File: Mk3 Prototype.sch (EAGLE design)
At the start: 170 parts, among them IC2 CC3100, IC3 S25FL216K0PMFI011, IC4 STM32F401V, IC6 AP3419, J1 ZX62-AB-5PA(11), J2 SWD_SHROUD, J7 SFV30R-2STE1HLF, Q1 BSS84W, Q11 BSS84W, Q12 2N7002KW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

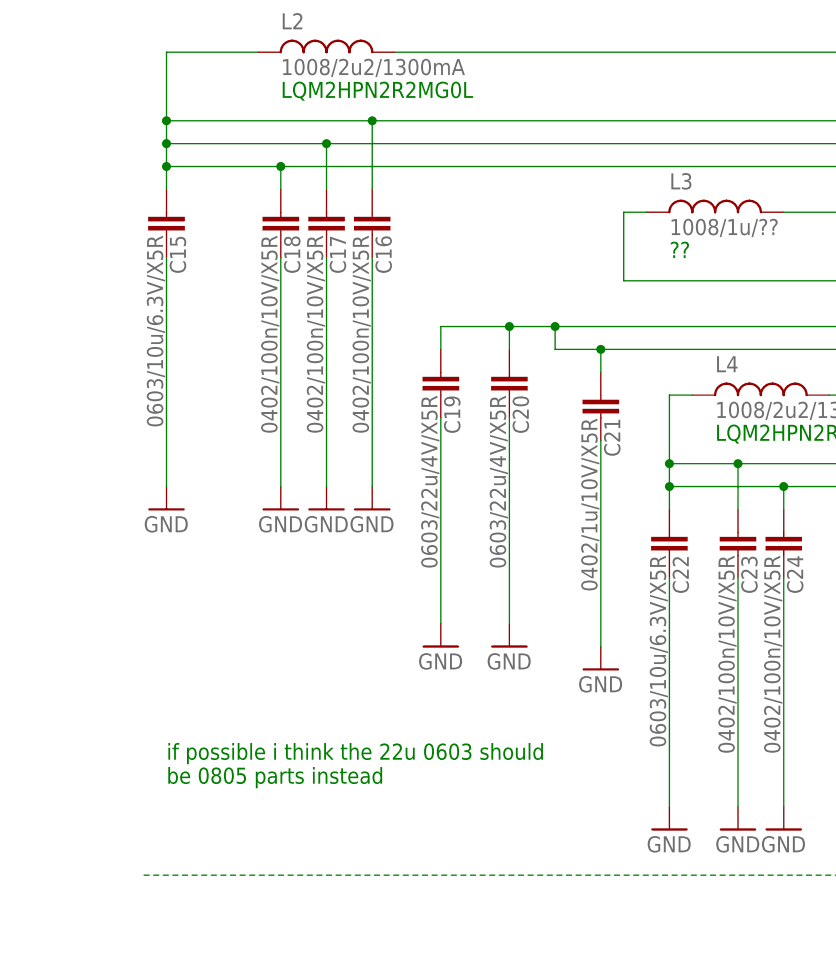
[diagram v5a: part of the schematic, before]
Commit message: some more power routing for the cc
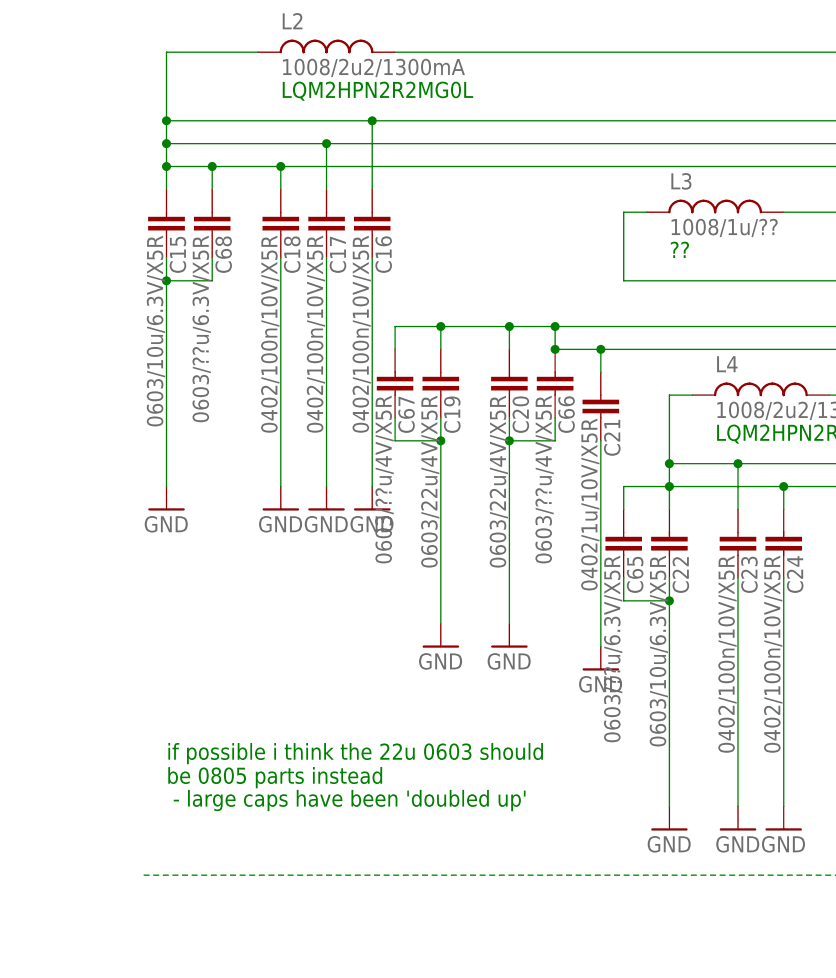
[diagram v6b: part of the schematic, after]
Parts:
- added C65, C68: 0603/??u/6.3V/X5R, TiLDA Mk3 Parts:C-EUC0603K-SMALL
- added C66, C67: 0603/??u/4V/X5R, TiLDA Mk3 Parts:C-EUC0603K-SMALL
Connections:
- net GND: now also C65.1, C66.1, C67.1, C68.1
- net N$17: now also C66.2, C67.2
- net N$18: now also C68.2
- net N$22: now also C65.2
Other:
- note added: "- large caps have been 'doubled up'"
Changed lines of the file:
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@@
 <part name="GND97" library="TiLDA Mk3 Parts" deviceset="GND" device=""/>
 <part name="+3V21" library="supply1" deviceset="+3V3" device=""/>
+<part name="C65" library="TiLDA Mk3 Parts" deviceset="C-EU" device="C0603K-SMALL" value="0603/??u/6.3V/X5R"/>
+<part name="C66" library="TiLDA Mk3 Parts" deviceset="C-EU" device="C0603K-SMALL" value="0603/??u/4V/X5R"/>
+<part name="C67" library="TiLDA Mk3 Parts" deviceset="C-EU" device="C0603K-SMALL" value="0603/??u/4V/X5R"/>
+<part name="C68" library="TiLDA Mk3 Parts" deviceset="C-EU" device="C0603K-SMALL" value="0603/??u/6.3V/X5R"/>
 </parts>
 <sheets>
@@
 <text x="741.68" y="246.38" size="1.778" layer="91">spec</text>
 <text x="797.56" y="177.8" size="2.54" layer="94">see if a resistor is needed on the stm32 crytal</text>
+<text x="408.94" y="157.48" size="1.778" layer="91"> - large caps have been 'doubled up'</text>
 </plain>
 <instances>
@@
 <instance part="GND97" gate="1" x="543.56" y="121.92" rot="R90"/>
 <instance part="+3V21" gate="G$1" x="701.04" y="162.56"/>
+<instance part="C65" gate="G$1" x="459.74" y="185.42" rot="R180"/>
+<instance part="C66" gate="G$1" x="452.12" y="203.2" rot="R180"/>
+<instance part="C67" gate="G$1" x="434.34" y="203.2" rot="R180"/>
+<instance part="C68" gate="G$1" x="414.02" y="220.98" rot="R180"/>
 </instances>
 <busses>
@@
 <segment>
 <pinref part="C15" gate="G$1" pin="1"/>
-<wire x1="408.94" y1="218.44" x2="408.94" y2="193.04" width="0.1524" layer="91"/>
+<wire x1="408.94" y1="218.44" x2="408.94" y2="215.9" width="0.1524" layer="91"/>
 <pinref part="GND28" gate="1" pin="GND"/>
+<pinref part="C68" gate="G$1" pin="1"/>
+<wire x1="408.94" y1="215.9" x2="408.94" y2="193.04" width="0.1524" layer="91"/>
+<wire x1="414.02" y1="218.44" x2="414.02" y2="215.9" width="0.1524" layer="91"/>
+<wire x1="414.02" y1="215.9" x2="408.94" y2="215.9" width="0.1524" layer="91"/>
+<junction x="408.94" y="215.9"/>
 </segment>
 <segment>
@@
 <pinref part="C19" gate="G$1" pin="1"/>
 <pinref part="GND29" gate="1" pin="GND"/>
-<wire x1="439.42" y1="177.8" x2="439.42" y2="200.66" width="0.1524" layer="91"/>
+<wire x1="439.42" y1="177.8" x2="439.42" y2="198.12" width="0.1524" layer="91"/>
+<pinref part="C67" gate="G$1" pin="1"/>
+<wire x1="439.42" y1="198.12" x2="439.42" y2="200.66" width="0.1524" layer="91"/>
+<wire x1="434.34" y1="200.66" x2="434.34" y2="198.12" width="0.1524" layer="91"/>
+<wire x1="434.34" y1="198.12" x2="439.42" y2="198.12" width="0.1524" layer="91"/>
+<junction x="439.42" y="198.12"/>
 </segment>
 <segment>
 <pinref part="C20" gate="G$1" pin="1"/>
 <pinref part="GND30" gate="1" pin="GND"/>
-<wire x1="447.04" y1="177.8" x2="447.04" y2="200.66" width="0.1524" layer="91"/>
+<wire x1="447.04" y1="177.8" x2="447.04" y2="198.12" width="0.1524" layer="91"/>
+<pinref part="C66" gate="G$1" pin="1"/>
+<wire x1="447.04" y1="198.12" x2="447.04" y2="200.66" width="0.1524" layer="91"/>
+<wire x1="452.12" y1="200.66" x2="452.12" y2="198.12" width="0.1524" layer="91"/>
+<wire x1="452.12" y1="198.12" x2="447.04" y2="198.12" width="0.1524" layer="91"/>
+<junction x="447.04" y="198.12"/>
 </segment>
 <segment>
@@
 <pinref part="C22" gate="G$1" pin="1"/>
 <pinref part="GND32" gate="1" pin="GND"/>
-<wire x1="464.82" y1="157.48" x2="464.82" y2="182.88" width="0.1524" layer="91"/>
+<wire x1="464.82" y1="157.48" x2="464.82" y2="180.34" width="0.1524" layer="91"/>
+<pinref part="C65" gate="G$1" pin="1"/>
+<wire x1="464.82" y1="180.34" x2="464.82" y2="182.88" width="0.1524" layer="91"/>
+<wire x1="459.74" y1="182.88" x2="459.74" y2="180.34" width="0.1524" layer="91"/>
+<wire x1="459.74" y1="180.34" x2="464.82" y2="180.34" width="0.1524" layer="91"/>
+<junction x="464.82" y="180.34"/>
 </segment>
 <segment>
@@
 <wire x1="495.3" y1="228.6" x2="421.64" y2="228.6" width="0.1524" layer="91"/>
 <pinref part="C15" gate="G$1" pin="2"/>
-<wire x1="421.64" y1="228.6" x2="408.94" y2="228.6" width="0.1524" layer="91"/>
+<wire x1="421.64" y1="228.6" x2="414.02" y2="228.6" width="0.1524" layer="91"/>
+<wire x1="414.02" y1="228.6" x2="408.94" y2="228.6" width="0.1524" layer="91"/>
 <wire x1="408.94" y1="226.06" x2="408.94" y2="228.6" width="0.1524" layer="91"/>
 <pinref part="IC2" gate="_POWER" pin="VDD_ANA1"/>
@@
 <pinref part="IC2" gate="_POWER" pin="LDO_IN2"/>
 <pinref part="IC2" gate="_POWER" pin="LDO_IN1"/>
+<pinref part="C68" gate="G$1" pin="2"/>
+<wire x1="414.02" y1="226.06" x2="414.02" y2="228.6" width="0.1524" layer="91"/>
+<junction x="414.02" y="228.6"/>
 </segment>
 </net>
@@
 <pinref part="IC2" gate="_POWER" pin="VDD_PA_IN"/>
 <pinref part="IC2" gate="_POWER" pin="DCDC_PA_OUT"/>
+<pinref part="C66" gate="G$1" pin="2"/>
+<junction x="452.12" y="208.28"/>
+<pinref part="C67" gate="G$1" pin="2"/>
+<wire x1="434.34" y1="208.28" x2="434.34" y2="210.82" width="0.1524" layer="91"/>
+<wire x1="434.34" y1="210.82" x2="439.42" y2="210.82" width="0.1524" layer="91"/>
+<junction x="439.42" y="210.82"/>
 </segment>
 </net>
@@
 <pinref part="IC2" gate="_POWER" pin="VDD_DIG1"/>
 <pinref part="IC2" gate="_POWER" pin="VDD_DIG2"/>
-</segment>
-</net>
+<pinref part="C65" gate="G$1" pin="2"/>
+<wire x1="459.74" y1="190.5" x2="459.74" y2="193.04" width="0.1524" layer="91"/>
+<wire x1="459.74" y1="193.04" x2="464.82" y2="193.04" width="0.1524" layer="91"/>
+</segment>
+</net>

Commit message: added low voltage cutoff
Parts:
- added C69: 1n, TiLDA Mk3 Parts:C-EUC1206K
- added IC1: BD49XXX, TiLDA Mk3 Parts:BD49XXX
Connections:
- new net N$12: C69.1, IC1.OUT, IC6.EN
- net GND: now also C69.2, IC1.GND
- net V_UNREG: now also IC1.VDD; no longer IC6.EN
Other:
- note added: "- needed with low voltage cutoff?"
- note added: "3.6V version"
- note added: "will probably want LPF to add a delay"
- note removed: "regulator"
- moved on the sheet: C58, C59, C60, C61, IC6, L7, R31, R32
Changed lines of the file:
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@@
 <part name="C67" library="TiLDA Mk3 Parts" deviceset="C-EU" device="C0603K-SMALL" value="0603/??u/4V/X5R"/>
 <part name="C68" library="TiLDA Mk3 Parts" deviceset="C-EU" device="C0603K-SMALL" value="0603/??u/6.3V/X5R"/>
+<part name="IC1" library="TiLDA Mk3 Parts" deviceset="BD49XXX" device=""/>
+<part name="GND98" library="TiLDA Mk3 Parts" deviceset="GND" device=""/>
+<part name="C69" library="TiLDA Mk3 Parts" deviceset="C-EU" device="C1206K" value="1n"/>
+<part name="GND99" library="TiLDA Mk3 Parts" deviceset="GND" device=""/>
 </parts>
 <sheets>
@@
 <text x="500.38" y="25.4" size="1.778" layer="91" rot="MR270">will probably want changing
  to the smaller version</text>
-<text x="584.2" y="20.32" size="1.778" layer="91">regulator</text>
 <text x="548.64" y="43.18" size="1.778" layer="91" rot="R270">perhaps should
 look for a better
@@
 <text x="525.78" y="53.34" size="1.778" layer="91">spec</text>
 <text x="416.56" y="43.18" size="1.778" layer="91" rot="R90">polyfuse?</text>
-<text x="568.96" y="55.88" size="1.778" layer="91">not certain on this part -
+<text x="599.44" y="55.88" size="1.778" layer="91">not certain on this part -
 dropout unclear,
 needs lots of capacitance</text>
-<text x="599.44" y="48.26" size="1.778" layer="91">spec</text>
+<text x="629.92" y="48.26" size="1.778" layer="91">spec</text>
 <text x="535.94" y="63.5" size="1.778" layer="91">spec</text>
 <text x="551.18" y="55.88" size="1.778" layer="91" rot="R90">spec</text>
@@
 <text x="797.56" y="177.8" size="2.54" layer="94">see if a resistor is needed on the stm32 crytal</text>
 <text x="408.94" y="157.48" size="1.778" layer="91"> - large caps have been 'doubled up'</text>
+<text x="571.5" y="25.4" size="1.778" layer="91">3.6V version</text>
+<text x="579.12" y="7.62" size="1.778" layer="91">will probably want LPF to add a delay</text>
+<wire x1="589.28" y1="10.16" x2="581.66" y2="10.16" width="0.1524" layer="97"/>
+<wire x1="581.66" y1="10.16" x2="581.66" y2="33.02" width="0.1524" layer="97"/>
+<text x="297.18" y="243.84" size="1.778" layer="91">- needed with low voltage cutoff?</text>
 </plain>
 <instances>
@@
 <instance part="R18" gate="G$1" x="441.96" y="43.18" rot="R180"/>
 <instance part="S5" gate="1" x="551.18" y="45.72" rot="R180"/>
-<instance part="+3V6" gate="G$1" x="635" y="45.72" rot="R270"/>
+<instance part="+3V6" gate="G$1" x="665.48" y="45.72" rot="R270"/>
 <instance part="C38" gate="G$1" x="434.34" y="35.56" rot="R180"/>
 <instance part="GND62" gate="1" x="434.34" y="27.94"/>
@@
 <instance part="GND87" gate="1" x="535.94" y="10.16"/>
 <instance part="GND88" gate="1" x="520.7" y="10.16"/>
-<instance part="IC6" gate="G$1" x="579.12" y="45.72"/>
-<instance part="GND89" gate="1" x="581.66" y="27.94"/>
-<instance part="R31" gate="G$1" x="609.6" y="40.64" rot="R270"/>
-<instance part="R32" gate="G$1" x="609.6" y="30.48" rot="R270"/>
-<instance part="GND90" gate="1" x="609.6" y="22.86"/>
-<instance part="L7" gate="G$1" x="601.98" y="45.72" rot="R90"/>
-<instance part="C58" gate="G$1" x="617.22" y="33.02"/>
-<instance part="C59" gate="G$1" x="622.3" y="33.02"/>
-<instance part="C60" gate="G$1" x="627.38" y="33.02"/>
-<instance part="GND91" gate="1" x="617.22" y="25.4"/>
-<instance part="GND92" gate="1" x="622.3" y="25.4"/>
-<instance part="GND93" gate="1" x="627.38" y="25.4"/>
-<instance part="C61" gate="G$1" x="566.42" y="33.02"/>
-<instance part="GND94" gate="1" x="566.42" y="25.4"/>
+<instance part="IC6" gate="G$1" x="609.6" y="45.72"/>
+<instance part="GND89" gate="1" x="612.14" y="27.94"/>
+<instance part="R31" gate="G$1" x="640.08" y="40.64" rot="R270"/>
+<instance part="R32" gate="G$1" x="640.08" y="30.48" rot="R270"/>
+<instance part="GND90" gate="1" x="640.08" y="22.86"/>
+<instance part="L7" gate="G$1" x="632.46" y="45.72" rot="R90"/>
+<instance part="C58" gate="G$1" x="647.7" y="33.02"/>
+<instance part="C59" gate="G$1" x="652.78" y="33.02"/>
+<instance part="C60" gate="G$1" x="657.86" y="33.02"/>
+<instance part="GND91" gate="1" x="647.7" y="25.4"/>
+<instance part="GND92" gate="1" x="652.78" y="25.4"/>
+<instance part="GND93" gate="1" x="657.86" y="25.4"/>
+<instance part="C61" gate="G$1" x="596.9" y="27.94"/>
+<instance part="GND94" gate="1" x="596.9" y="20.32"/>
 <instance part="D4" gate="G$1" x="538.48" y="55.88"/>
 <instance part="D1" gate="G$1" x="538.48" y="66.04" rot="R180"/>
@@
 <instance part="C67" gate="G$1" x="434.34" y="203.2" rot="R180"/>
 <instance part="C68" gate="G$1" x="414.02" y="220.98" rot="R180"/>
+<instance part="IC1" gate="G$1" x="576.58" y="35.56"/>
+<instance part="GND98" gate="1" x="566.42" y="27.94"/>
+<instance part="C69" gate="G$1" x="591.82" y="27.94"/>
+<instance part="GND99" gate="1" x="591.82" y="20.32"/>
 </instances>
 <busses>
@@
 <pinref part="GND97" gate="1" pin="GND"/>
 </segment>
+<segment>
+<pinref part="IC1" gate="G$1" pin="GND"/>
+<pinref part="GND98" gate="1" pin="GND"/>
+<wire x1="568.96" y1="33.02" x2="566.42" y2="33.02" width="0.1524" layer="91"/>
+<wire x1="566.42" y1="33.02" x2="566.42" y2="30.48" width="0.1524" layer="91"/>
+</segment>
+<segment>
+<pinref part="C69" gate="G$1" pin="2"/>
+<pinref part="GND99" gate="1" pin="GND"/>
+</segment>
 </net>
 <net name="F1" class="0">
@@
 <pinref part="+3V6" gate="G$1" pin="+3V3"/>
 <pinref part="R31" gate="G$1" pin="1"/>
-<wire x1="609.6" y1="45.72" x2="617.22" y2="45.72" width="0.1524" layer="91"/>
+<wire x1="640.08" y1="45.72" x2="647.7" y2="45.72" width="0.1524" layer="91"/>
 <pinref part="L7" gate="G$1" pin="2"/>
-<junction x="609.6" y="45.72"/>
+<junction x="640.08" y="45.72"/>
 <pinref part="C58" gate="G$1" pin="1"/>
-<wire x1="627.38" y1="45.72" x2="632.46" y2="45.72" width="0.1524" layer="91"/>
-<wire x1="617.22" y1="35.56" x2="617.22" y2="45.72" width="0.1524" layer="91"/>
+<wire x1="657.86" y1="45.72" x2="662.94" y2="45.72" width="0.1524" layer="91"/>
+<wire x1="647.7" y1="35.56" x2="647.7" y2="45.72" width="0.1524" layer="91"/>
 <pinref part="C59" gate="G$1" pin="1"/>
-<wire x1="617.22" y1="45.72" x2="622.3" y2="45.72" width="0.1524" layer="91"/>
-<wire x1="622.3" y1="45.72" x2="622.3" y2="35.56" width="0.1524" layer="91"/>
+<wire x1="647.7" y1="45.72" x2="652.78" y2="45.72" width="0.1524" layer="91"/>
+<wire x1="652.78" y1="45.72" x2="652.78" y2="35.56" width="0.1524" layer="91"/>
 <pinref part="C60" gate="G$1" pin="1"/>
-<wire x1="622.3" y1="45.72" x2="627.38" y2="45.72" width="0.1524" layer="91"/>
-<wire x1="627.38" y1="45.72" x2="627.38" y2="35.56" width="0.1524" layer="91"/>
-<junction x="617.22" y="45.72"/>
-<junction x="622.3" y="45.72"/>
-<junction x="627.38" y="45.72"/>
+<wire x1="652.78" y1="45.72" x2="657.86" y2="45.72" width="0.1524" layer="91"/>
+<wire x1="657.86" y1="45.72" x2="657.86" y2="35.56" width="0.1524" layer="91"/>
+<junction x="647.7" y="45.72"/>
+<junction x="652.78" y="45.72"/>
+<junction x="657.86" y="45.72"/>
 </segment>
 <segment>
@@
 <label x="556.26" y="45.72" size="1.778" layer="95" rot="R270" xref="yes"/>
 <pinref part="IC6" gate="G$1" pin="VIN"/>
-<wire x1="568.96" y1="45.72" x2="566.42" y2="45.72" width="0.1524" layer="91"/>
-<pinref part="IC6" gate="G$1" pin="EN"/>
+<wire x1="599.44" y1="45.72" x2="596.9" y2="45.72" width="0.1524" layer="91"/>
+<wire x1="596.9" y1="45.72" x2="566.42" y2="45.72" width="0.1524" layer="91"/>
 <wire x1="566.42" y1="45.72" x2="556.26" y2="45.72" width="0.1524" layer="91"/>
-<wire x1="568.96" y1="40.64" x2="566.42" y2="40.64" width="0.1524" layer="91"/>
-<wire x1="566.42" y1="40.64" x2="566.42" y2="45.72" width="0.1524" layer="91"/>
-<junction x="566.42" y="45.72"/>
-<pinref part="C61" gate="G$1" pin="1"/>
-<wire x1="566.42" y1="35.56" x2="566.42" y2="40.64" width="0.1524" layer="91"/>
-<junction x="566.42" y="40.64"/>
 <pinref part="D1" gate="G$1" pin="A"/>
 <wire x1="541.02" y1="66.04" x2="556.26" y2="66.04" width="0.1524" layer="91"/>
@@
 <wire x1="553.72" y1="45.72" x2="556.26" y2="45.72" width="0.1524" layer="91"/>
 <junction x="556.26" y="45.72"/>
+<pinref part="IC1" gate="G$1" pin="VDD"/>
+<wire x1="568.96" y1="38.1" x2="566.42" y2="38.1" width="0.1524" layer="91"/>
+<wire x1="566.42" y1="38.1" x2="566.42" y2="45.72" width="0.1524" layer="91"/>
+<junction x="566.42" y="45.72"/>
+<pinref part="C61" gate="G$1" pin="1"/>
+<wire x1="596.9" y1="30.48" x2="596.9" y2="45.72" width="0.1524" layer="91"/>
+<junction x="596.9" y="45.72"/>
 </segment>
 <segment>
@@
 <pinref part="R31" gate="G$1" pin="2"/>
 <pinref part="R32" gate="G$1" pin="1"/>
-<wire x1="609.6" y1="35.56" x2="601.98" y2="35.56" width="0.1524" layer="91"/>
-<wire x1="601.98" y1="35.56" x2="601.98" y2="40.64" width="0.1524" layer="91"/>
+<wire x1="640.08" y1="35.56" x2="632.46" y2="35.56" width="0.1524" layer="91"/>
+<wire x1="632.46" y1="35.56" x2="632.46" y2="40.64" width="0.1524" layer="91"/>
 <pinref part="IC6" gate="G$1" pin="FB"/>
-<wire x1="601.98" y1="40.64" x2="594.36" y2="40.64" width="0.1524" layer="91"/>
-<junction x="609.6" y="35.56"/>
+<wire x1="632.46" y1="40.64" x2="624.84" y2="40.64" width="0.1524" layer="91"/>
+<junction x="640.08" y="35.56"/>
 </segment>
 </net>
@@
 </segment>
 </net>
+<net name="N$12" class="0">
+<segment>
+<pinref part="IC6" gate="G$1" pin="EN"/>
+<wire x1="599.44" y1="40.64" x2="594.36" y2="40.64" width="0.1524" layer="91"/>
+<wire x1="594.36" y1="40.64" x2="594.36" y2="35.56" width="0.1524" layer="91"/>
+<pinref part="IC1" gate="G$1" pin="OUT"/>
+<pinref part="C69" gate="G$1" pin="1"/>
+<wire x1="591.82" y1="30.48" x2="591.82" y2="35.56" width="0.1524" layer="91"/>
+<wire x1="591.82" y1="35.56" x2="594.36" y2="35.56" width="0.1524" layer="91"/>
+<junction x="591.82" y="35.56"/>
+</segment>
+</net>
